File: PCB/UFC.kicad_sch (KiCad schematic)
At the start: 85 parts, among them Q1 NMOS, Q2 NMOS, Q3 NMOS, Q4 NMOS, Q5 NMOS, Q6 NMOS, Q7 NMOS, Q8 NMOS

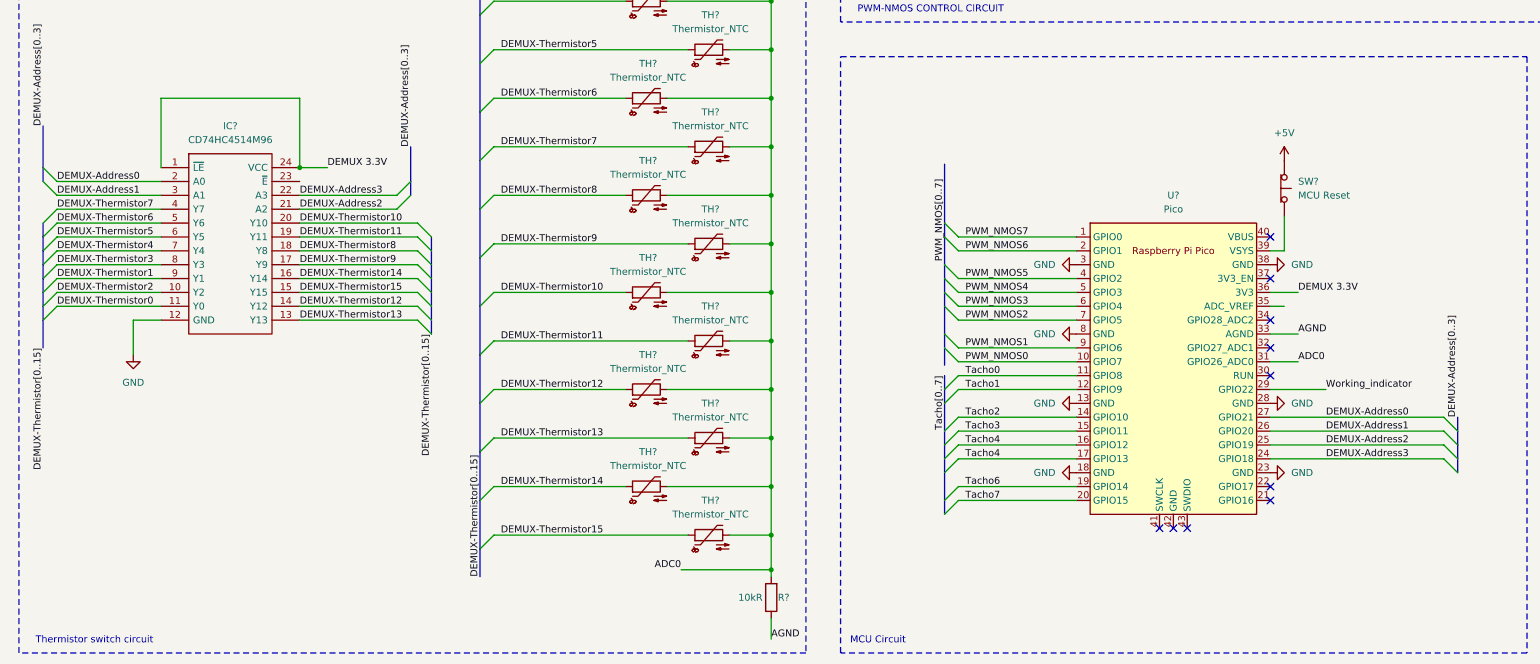
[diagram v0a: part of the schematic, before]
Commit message: Update UFC.kicad_sch
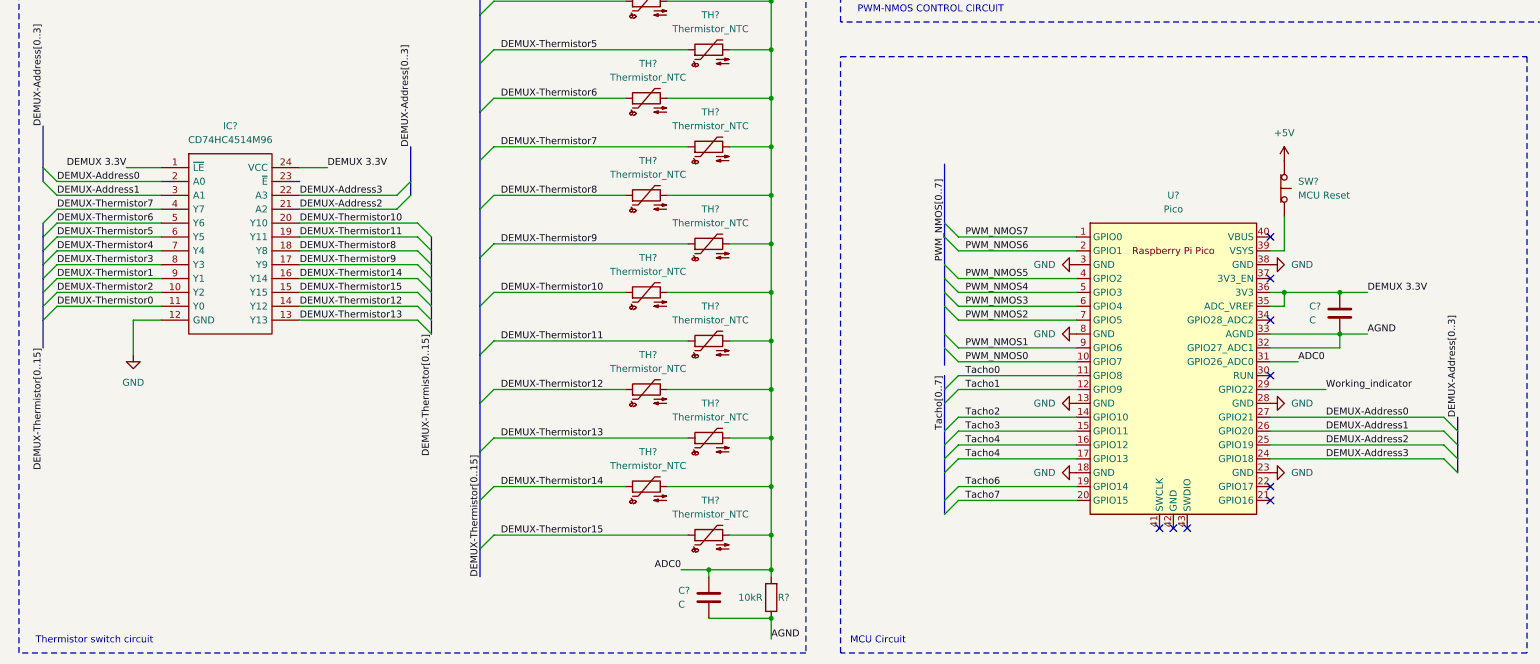
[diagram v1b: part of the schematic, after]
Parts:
- added C? (x2): C, symbol Device:C
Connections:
- net ADC0: now also C?.1
- net AGND: now also U?.32 (GPIO27_ADC1), C?.2, C?.2
- net DEMUX 3.3V: now also U?.35 (ADC_VREF), C?.1
- no-connect marks 10 -> 9

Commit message: npn
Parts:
- removed C? (x2): C, symbol Device:C
- removed Q1, Q2, Q3, Q4, Q5, Q6, Q7, Q8: NMOS, symbol Simulation_SPICE:NMOS
- added Q0, Q1, Q2, Q3, Q4, Q5, Q6, Q7: NPN, symbol Simulation_SPICE:NPN
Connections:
- net AGND: no longer U?.32 (GPIO27_ADC1)
- net DEMUX 3.3V: no longer U?.35 (ADC_VREF)
- net FAN_TACHO0: now also Q0.2 (B)
- net FAN_TACHO1: now also Q1.2 (B)
- net FAN_TACHO2: now also Q2.2 (B)
- net FAN_TACHO3: now also Q3.2 (B)
- net FAN_TACHO4: now also Q4.2 (B)
- net FAN_TACHO5: now also Q5.2 (B)
- net FAN_TACHO6: now also Q6.2 (B)
- net FAN_TACHO7: now also Q7.2 (B)
- net GND: now also Q0.3 (E), Q1.3 (E), Q2.3 (E), Q3.3 (E), Q4.3 (E), Q5.3 (E), Q6.3 (E), Q7.3 (E)
- net Tacho0: now also Q0.1 (C)
- net Tacho1: now also Q1.1 (C)
- net Tacho2: now also Q2.1 (C)
- net Tacho3: now also Q3.1 (C)
- net Tacho4: now also Q4.1 (C)
- net Tacho5: now also Q5.1 (C)
- net Tacho6: now also Q6.1 (C)
- net Tacho7: now also Q7.1 (C)
- no-connect marks 9 -> 10

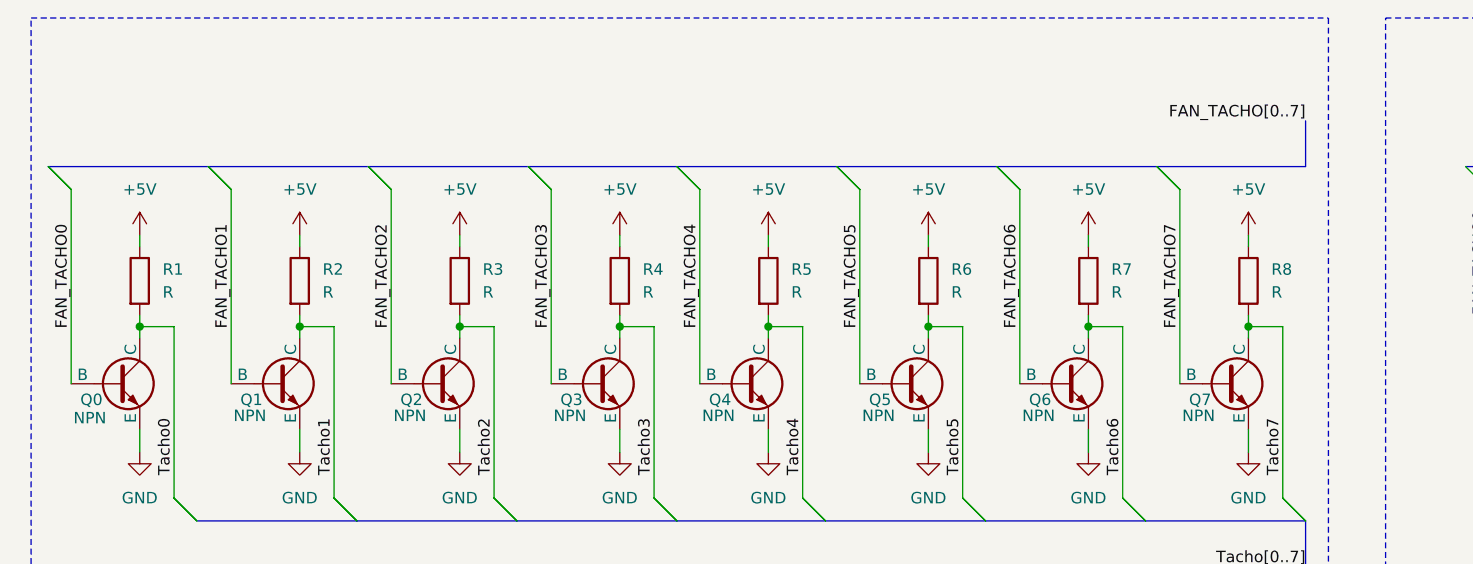
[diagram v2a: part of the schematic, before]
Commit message: Update UFC.kicad_sch
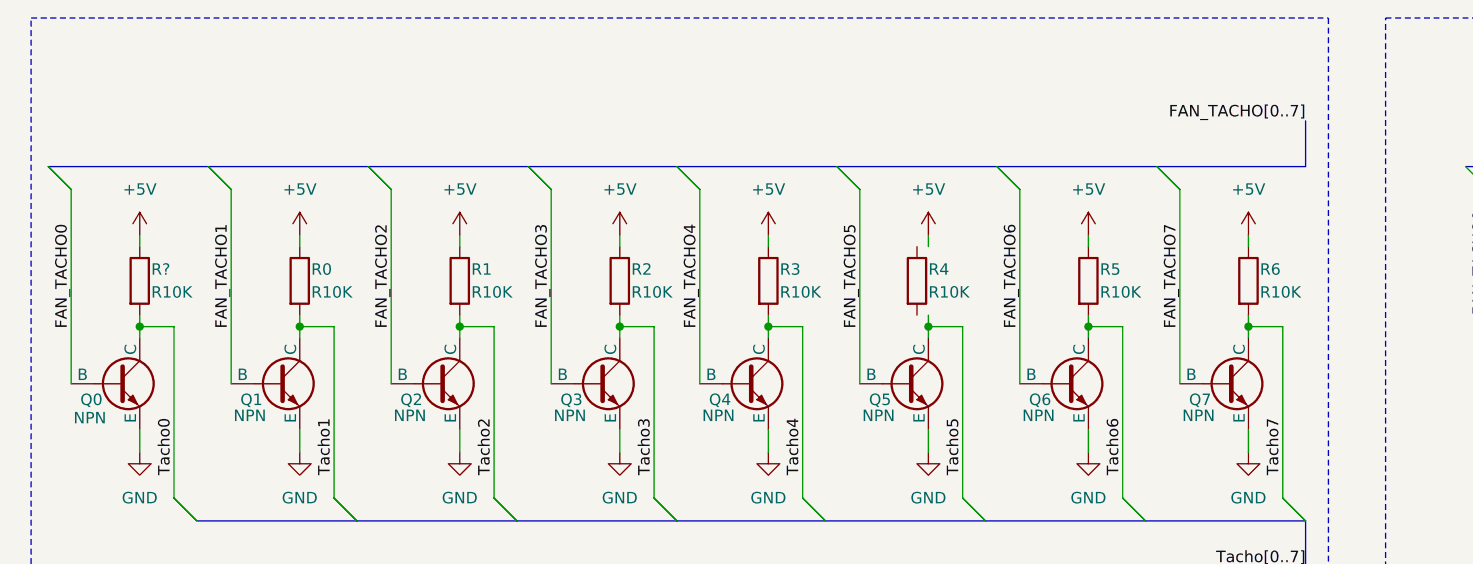
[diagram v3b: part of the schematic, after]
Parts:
- removed R7, R8: R, symbol Device:R
- added R0, R1: R10K, symbol Device:R
- R2, R3, R4, R5, R6: value R -> R10K
- R?: renamed from R1; value R -> R10K
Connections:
- net +5V: now also R0.1, R1.1; no longer R4.1
- net Tacho1: now also R0.2; no longer R2.2
- net Tacho2: now also R1.2; no longer R3.2
- net Tacho3: now also R2.2; no longer R4.2
- net Tacho4: now also R3.2; no longer R5.2
- net Tacho5: no longer R6.2
- net Tacho6: now also R5.2
- net Tacho7: now also R6.2

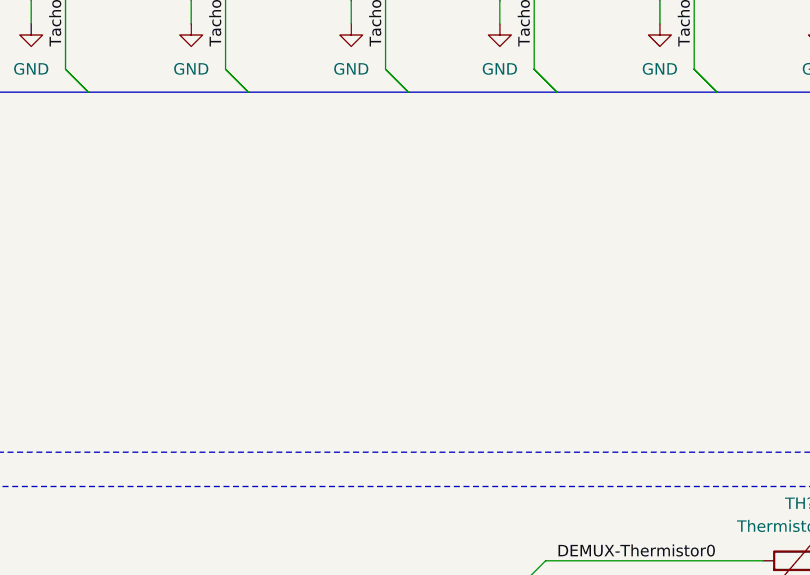
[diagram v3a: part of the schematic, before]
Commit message: Update UFC.kicad_sch
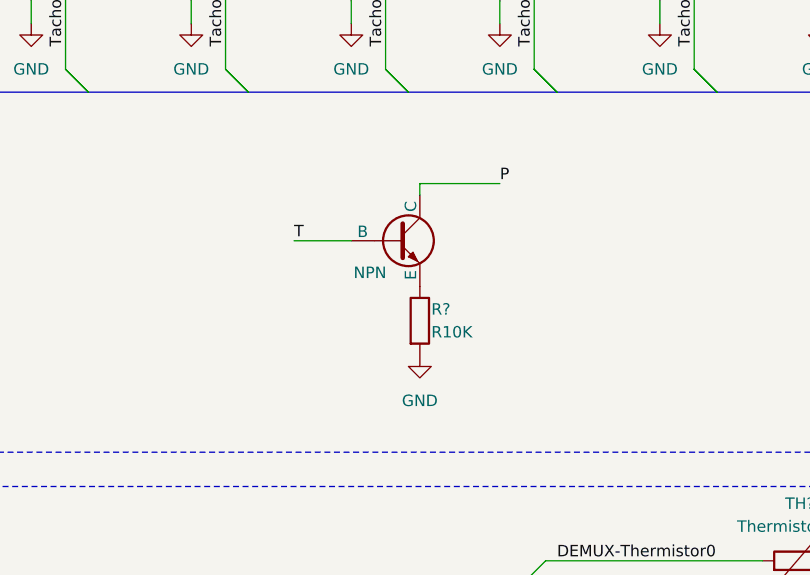
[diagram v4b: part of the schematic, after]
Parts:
- added Q?: NPN, symbol Simulation_SPICE:NPN
- added R?: R10K, symbol Device:R
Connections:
- net GND: now also R?.2
- new net: Q?.3 (E), R?.1
- new net P: Q?.1 (C)
- new net T: Q?.2 (B)

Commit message: WIP
Work in progress
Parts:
- removed IC?: CD74HC4514M96, SOIC127P1030X265-24N, symbol UFC_Lib:CD74HC4514M96
- added IC0, IC1: CD74HCT4067M, SOIC127P1030X265-24N, symbol UFC_Lib:CD74HCT4067M
- added R9: 10kR, symbol Device:R
- added TH0, TH10, TH12, TH14, TH16, TH18, TH2, TH20, TH22, TH24, TH26, TH28, TH30, TH4, TH6, TH8: Thermistor_NTC, symbol Device:Thermistor_NTC
- gave numbers to parts that had none: 71
- renumbered R0 to R1, R1 to R2, R2 to R3, R3 to R4, R4 to R5, R5 to R6, R6 to R7
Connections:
- net PWM-NMOS0 is gone; now on net PWM_NMOS0: R11.1, R19.2
- net PWM-NMOS1 is gone; now on net PWM_NMOS1: R12.1, R20.2
- net PWM-NMOS2 is gone; now on net PWM_NMOS2: R13.1, R21.2
- net PWM-NMOS3 is gone; now on net PWM_NMOS3: R14.1, R22.2
- net PWM-NMOS4 is gone; now on net PWM_NMOS4: R15.1, R23.2
- net PWM-NMOS5 is gone; now on net PWM_NMOS5: R16.1, R24.2
- net PWM-NMOS6 is gone; now on net PWM_NMOS6: R17.1, R25.2
- net PWM-NMOS7 is gone; now on net PWM_NMOS7: R18.1, R26.2
- net +5V: now also R5.1, IC0.24 (VCC), IC1.24 (VCC)
- net ADC0: now also R9.2, TH0.2, TH10.2, TH12.2, TH14.2, TH16.2, TH18.2, TH2.2, TH20.2, TH22.2, TH24.2, TH26.2, TH28.2, TH30.2, TH4.2, TH6.2, TH8.2; no longer R10.2, TH1.2, TH11.2, TH13.2, TH15.2, TH17.2, TH19.2, TH21.2, TH23.2, TH25.2, TH27.2, TH29.2, TH3.2, TH31.2, TH5.2, TH7.2, TH9.2
- net AGND: now also R9.1
- net DEMUX 3.3V: now also IC0.1 (COMMON_INPUT/OUTPUT), IC1.1 (COMMON_INPUT/OUTPUT)
- net DEMUX-Address0: now also IC0.10 (S0), IC1.10 (S0)
- net DEMUX-Address1: now also IC0.11 (S1), IC1.11 (S1)
- net DEMUX-Address2: now also IC0.14 (S2), IC1.14 (S2)
- net DEMUX-Address3: now also IC0.13 (S3), IC1.13 (S3)
- net DEMUX-Thermistor0: now also IC0.9 (I0), TH0.1; no longer TH1.1
- net DEMUX-Thermistor1: now also IC0.8 (I1), TH2.1; no longer TH3.1
- net DEMUX-Thermistor10: now also IC0.21 (I10), TH20.1; no longer TH21.1
- net DEMUX-Thermistor11: now also IC0.20 (I11), TH22.1; no longer TH23.1
- net DEMUX-Thermistor12: now also IC0.19 (I12), TH24.1; no longer TH25.1
- net DEMUX-Thermistor13: now also IC0.18 (I13), TH26.1; no longer TH27.1
- net DEMUX-Thermistor14: now also IC0.17 (I14), TH28.1; no longer TH29.1
- net DEMUX-Thermistor15: now also IC0.16 (I15), TH30.1; no longer TH31.1
- net DEMUX-Thermistor2: now also IC0.7 (I2), TH4.1; no longer TH5.1
- net DEMUX-Thermistor3: now also IC0.6 (I3), TH6.1; no longer TH7.1
- net DEMUX-Thermistor4: now also IC0.5 (I4), TH8.1; no longer TH9.1
- net DEMUX-Thermistor5: now also IC0.4 (I5), TH10.1; no longer TH11.1
- net DEMUX-Thermistor6: now also IC0.3 (I6), TH12.1; no longer TH13.1
- net DEMUX-Thermistor7: now also IC0.2 (I7), TH14.1; no longer TH15.1
- net DEMUX-Thermistor8: now also IC0.23 (I8), TH16.1; no longer TH17.1
- net DEMUX-Thermistor9: now also IC0.22 (I9), TH18.1; no longer TH19.1
- net GND: now also IC0.12 (GND), IC1.12 (GND)
- net PWM_NMOS0: now also U0.1 (GPIO0); no longer U0.10 (GPIO7)
- net PWM_NMOS1: now also U0.2 (GPIO1); no longer U0.9 (GPIO6)
- net PWM_NMOS2: now also U0.4 (GPIO2); no longer U0.7 (GPIO5)
- net PWM_NMOS3: now also U0.5 (GPIO3); no longer U0.6 (GPIO4)
- net PWM_NMOS4: now also U0.6 (GPIO4); no longer U0.5 (GPIO3)
- net PWM_NMOS5: now also U0.7 (GPIO5); no longer U0.4 (GPIO2)
- net PWM_NMOS6: now also U0.9 (GPIO6); no longer U0.2 (GPIO1)
- net PWM_NMOS7: now also U0.10 (GPIO7); no longer U0.1 (GPIO0)
- net Relay_open: now also Q12.3 (S), R22.1
- net Tacho5: now also R5.2
- net DEMUX(0-15)_Disable: now reaches U0.21 (GPIO16)
- net DEMUX(0-15)_Disable: now also IC0.15 (~{E})
- net DEMUX(16-31)_Disable: now reaches U0.22 (GPIO17)
- net DEMUX(16-31)_Disable: now also IC1.15 (~{E})
- net ADC1: now reaches U0.32 (GPIO27_ADC1)
- net ADC1: now also R10.2, TH1.2, TH11.2, TH13.2, TH15.2, TH17.2, TH19.2, TH21.2, TH23.2, TH25.2, TH27.2, TH29.2, TH3.2, TH31.2, TH5.2, TH7.2, TH9.2
- new net DEMUX-Thermistor16: IC1.9 (I0), TH1.1
- new net DEMUX-Thermistor17: IC1.8 (I1), TH3.1
- new net DEMUX-Thermistor18: IC1.7 (I2), TH5.1
- new net DEMUX-Thermistor19: IC1.6 (I3), TH7.1
- new net DEMUX-Thermistor20: IC1.5 (I4), TH9.1
- new net DEMUX-Thermistor21: IC1.4 (I5), TH11.1
- new net DEMUX-Thermistor22: IC1.3 (I6), TH13.1
- new net DEMUX-Thermistor23: IC1.2 (I7), TH15.1
- new net DEMUX-Thermistor24: IC1.23 (I8), TH17.1
- new net DEMUX-Thermistor25: IC1.22 (I9), TH19.1
- new net DEMUX-Thermistor26: IC1.21 (I10), TH21.1
- new net DEMUX-Thermistor27: IC1.20 (I11), TH23.1
- new net DEMUX-Thermistor28: IC1.19 (I12), TH25.1
- new net DEMUX-Thermistor29: IC1.18 (I13), TH27.1
- new net DEMUX-Thermistor30: IC1.17 (I14), TH29.1
- new net DEMUX-Thermistor31: IC1.16 (I15), TH31.1
- no-connect marks 10 -> 8
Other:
- note added: "Thermistor (0-15) DEMUX circuit"
- note added: "Thermistor (16-31) DEMUX circuit"
- note added: "Thermistors (0-15)"
- note added: "Thermistors (16-31)"
- note removed: "Thermistor switch circuit"
- moved on the sheet: D0, D1, D2, D3, D4, D5, D6, D7, D8, D9, F0, K0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

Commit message: footprinty machen
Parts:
- removed Q0, Q1, Q2, Q3, Q4, Q5, Q6, Q7, Q8: NPN, symbol Simulation_SPICE:NPN
- removed Q10, Q11, Q12, Q13, Q14, Q15, Q16: NMOS, symbol Simulation_SPICE:NMOS
- removed R26: 4.7KR, symbol Device:R
- added C0, C1, C2, C3, C4, C5, C6, C7: 4.7u, Capacitor_THT:CP_Radial_D5.0mm_P2.00mm, symbol Device:C
- added Q0, Q1, Q2, Q3, Q4, Q5, Q6: NMOS, Package_TO_SOT_SMD:SOT-23_Handsoldering, symbol Simulation_SPICE:NMOS
- Q9: footprint (none) -> Package_TO_SOT_SMD:SOT-23_Handsoldering
- R0, R1, R2, R3, R4, R5, R7: value R10K -> R300; footprint (none) -> Resistor_SMD:R_0603_1608Metric_Pad0.98x0.95mm_HandSolder
- R19, R20, R21, R22, R23, R24, R25: footprint (none) -> Capacitor_SMD:C_0402_1005Metric_Pad0.74x0.62mm_HandSolder
- R6: value R10K -> R300; footprint (none) -> Crystal:Crystal_SMD_0603-2Pin_6.0x3.5mm_HandSoldering
- R8: value R10K -> 4.7KR; footprint (none) -> Capacitor_SMD:C_0402_1005Metric_Pad0.74x0.62mm_HandSolder
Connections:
- net +5V: no longer R0.1, R1.1, R2.1, R3.1, R4.1, R5.1, R6.1, R7.1
- net GND: now also C0.1, C1.1, C2.1, C3.1, C4.1, C5.1, C6.1, C7.1; no longer R8.2
- net NMOS-FAN1: now also Q0.1 (D)
- net NMOS-FAN2: now also Q1.1 (D)
- net NMOS-FAN3: now also Q2.1 (D)
- net NMOS-FAN4: now also Q3.1 (D)
- net NMOS-FAN5: now also Q4.1 (D)
- net NMOS-FAN6: now also Q5.1 (D)
- net NMOS-FAN7: now also Q6.1 (D)
- net PWM_NMOS1: now also R8.2; no longer R20.2
- net PWM_NMOS2: now also R20.2; no longer R21.2
- net PWM_NMOS3: now also R21.2; no longer R22.2
- net PWM_NMOS4: now also R22.2; no longer R23.2
- net PWM_NMOS5: now also R23.2; no longer R24.2
- net PWM_NMOS6: now also R24.2; no longer R25.2
- net PWM_NMOS7: now also R25.2
- net Relay_open: now also R8.1, Q0.3 (S), Q1.3 (S), Q2.3 (S), Q3.3 (S), Q4.3 (S), Q5.3 (S), Q6.3 (S)
- net Tacho0: no longer R0.2
- net Tacho1: no longer R1.2
- net Tacho2: no longer R2.2
- net Tacho3: no longer R3.2
- net Tacho4: no longer R4.2
- net Tacho6: no longer R6.2
- net Tacho7: no longer R7.2
- net at R14.2: now also Q2.2 (G)
- net at R15.2: now also Q3.2 (G)
- net at R18.2: now also Q6.2 (G)
- net at R12.2: now also Q0.2 (G)
- net at R13.2: now also Q1.2 (G)
- net at R16.2: now also Q4.2 (G)
- net at R17.2: now also Q5.2 (G)
- net Tacho5: no longer names the net of R5.2
- net Tacho5: now also C5.2
- new net: C4.2, R4.2
- new net: C6.2, R6.2
- new net: C3.2, R3.2
- new net: C7.2, R7.2
- new net: C1.2, R1.2
- new net: C0.2, R0.2
- new net: C2.2, R2.2
